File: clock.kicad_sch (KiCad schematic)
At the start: 20 parts, among them Q3 DTC014T_SOT-416, U7 NB3L202KMN, U8 SN65LVDS1_SOIC, U9 Oscillator_27MHz_JU6, Y1 Oscillator_100MHz_NX324, Y2 Oscillator_26MHz_ESC_2520MV, Y3 Oscillator_125MHz_AX3DA

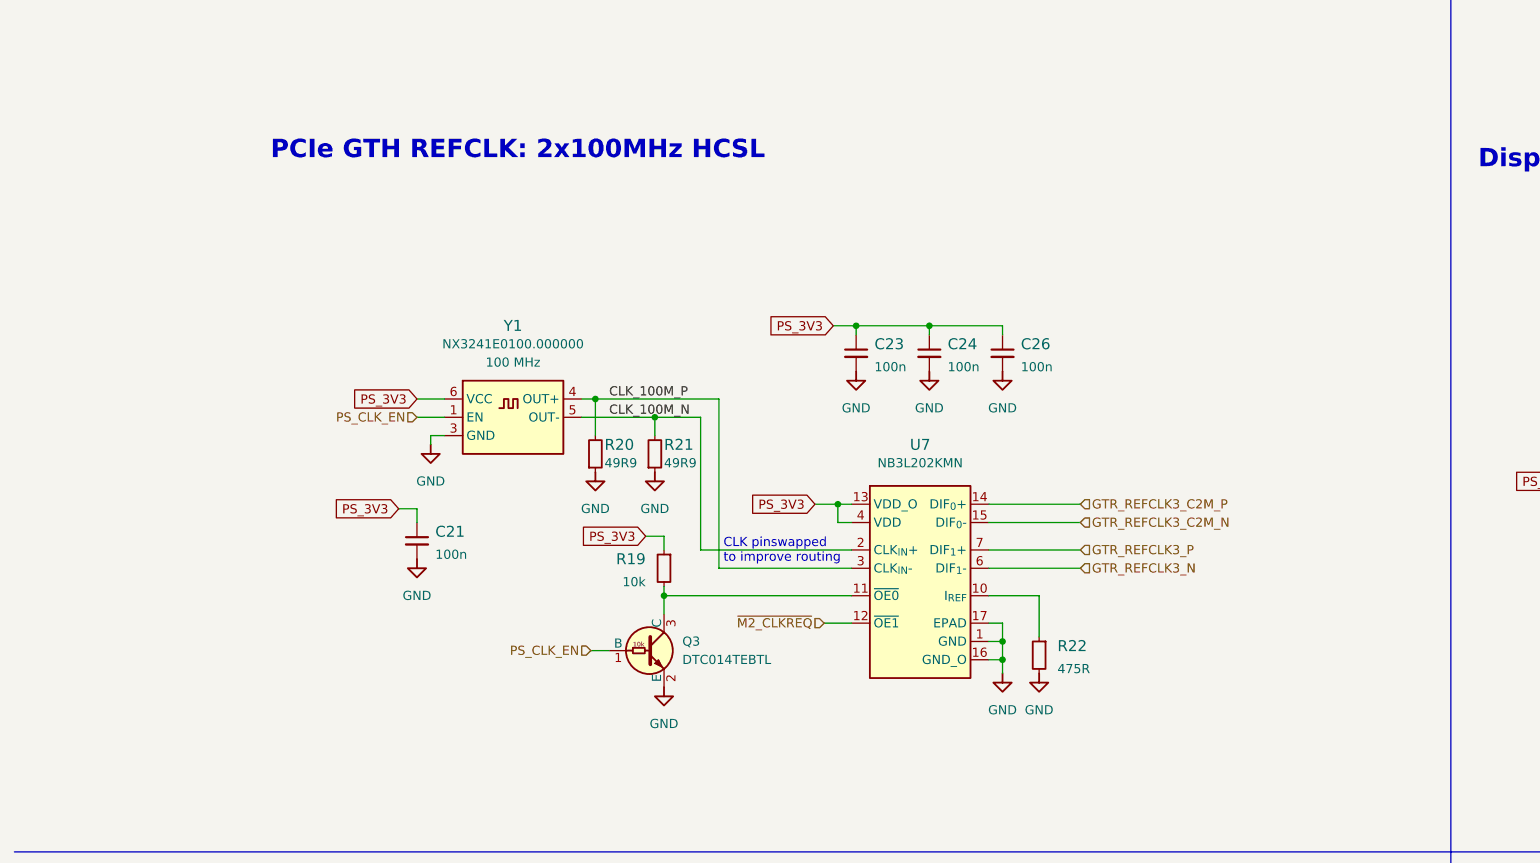
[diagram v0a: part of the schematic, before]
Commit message: PCIe clock termination fix
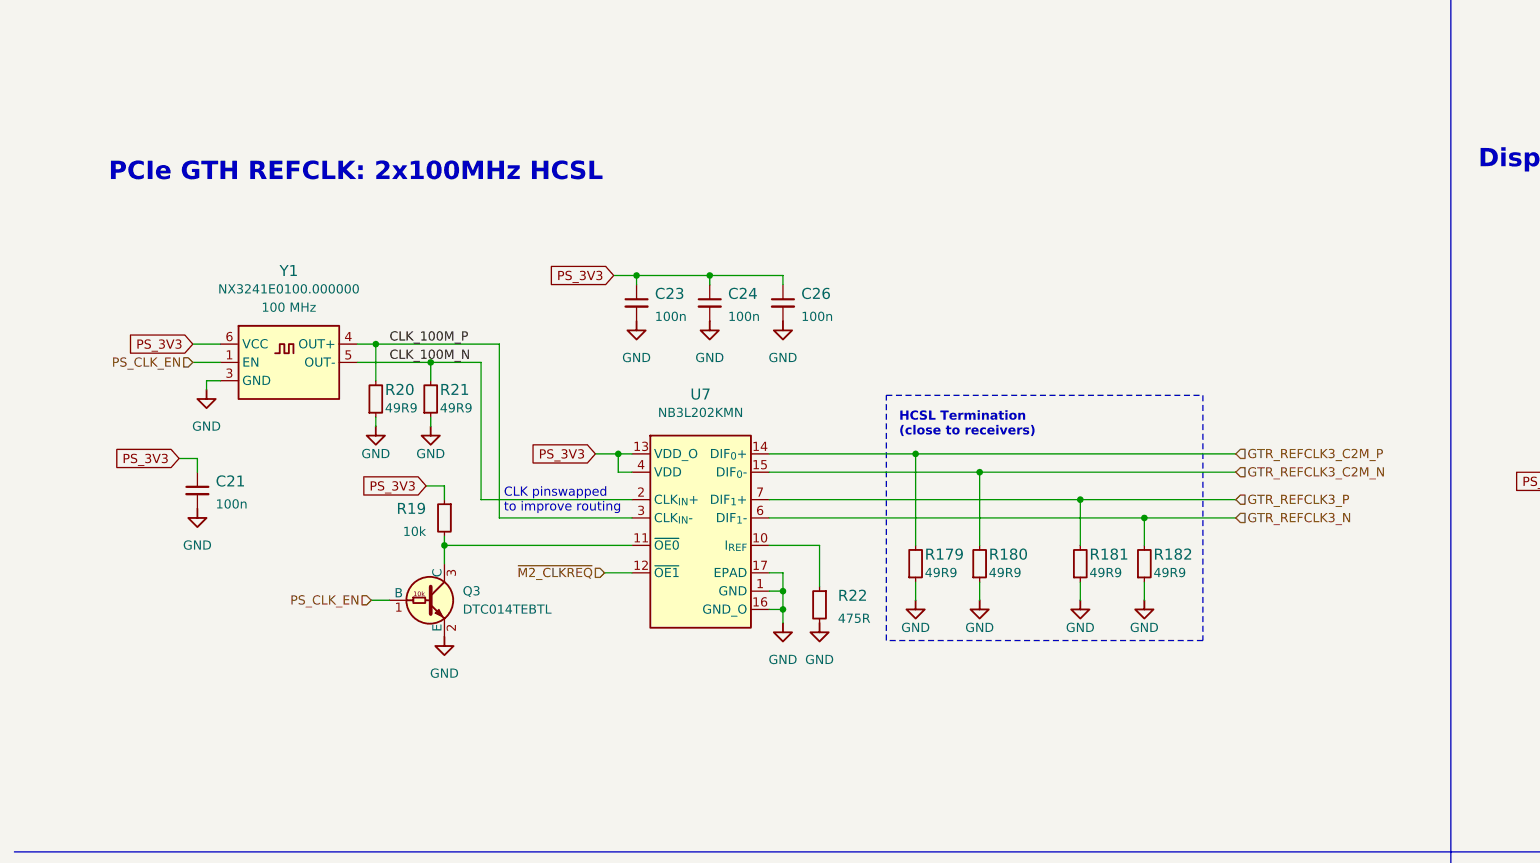
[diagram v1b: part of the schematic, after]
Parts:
- added R179, R180, R181, R182: R_49R9_0402, kria-k26-devboard-footprints:R_0402_1005Metric, symbol kria-k26-devboard:R_49R9_0402
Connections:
- net GND: now also R179.1, R180.1, R181.1, R182.1
- net GTR_REFCLK3_C2M_N: now also R180.2
- net GTR_REFCLK3_C2M_P: now also R179.2
- net GTR_REFCLK3_N: now also R182.2
- net GTR_REFCLK3_P: now also R181.2
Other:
- note added: "HCSL Termination (close to receivers)"
- moved on the sheet: C21, C23, C24, C26, Q3, R19, R20, R21, R22, U7, Y1
